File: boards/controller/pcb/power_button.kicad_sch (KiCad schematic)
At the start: 13 parts, among them Q6001 BSS138

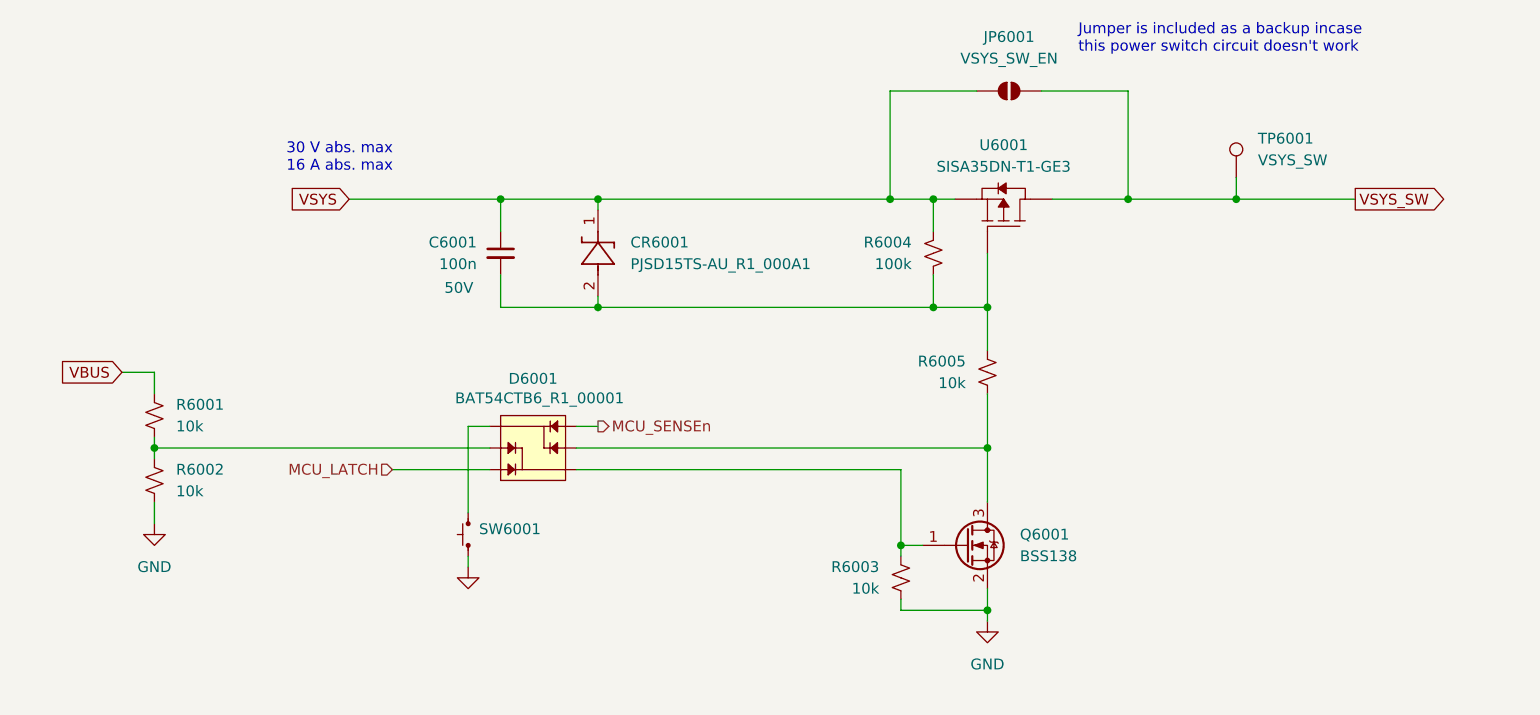
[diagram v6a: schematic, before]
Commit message: controller: Update BOM
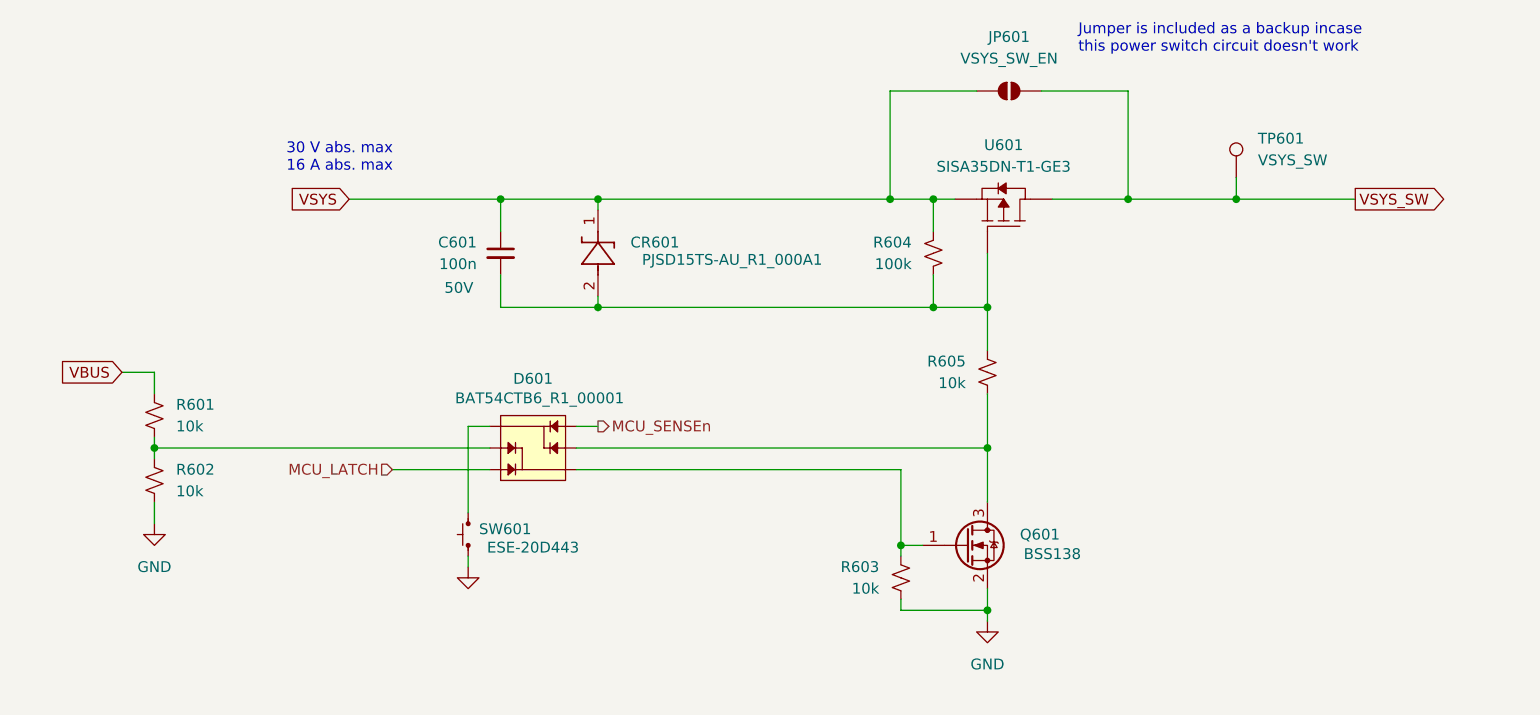
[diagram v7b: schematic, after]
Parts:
- CR601: renamed from CR6001; MPN (none) -> PJSD15TS-AU_R1_000A1
- Q601: renamed from Q6001; MPN (none) -> BSS138
- SW601: renamed from SW6001; MPN (none) -> ESE-20D443
- renumbered C6001 to C601, D6001 to D601, JP6001 to JP601, R6001 to R601, R6002 to R602, R6003 to R603, R6004 to R604, R6005 to R605, TP6001 to TP601, U6001 to U601
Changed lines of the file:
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@@
 		(on_board yes)
 		(dnp no)
-		(fields_autoplaced yes)
-		(property "Reference" "SW6001"
+		(property "Reference" "SW601"
 			(at 123.19 107.3149 90)
 			(effects
@@
 			)
 		)
+		(property "MPN" "ESE-20D443"
+			(at 129.54 109.474 90)
+			(effects
+				(font
+					(size 1.27 1.27)
+				)
+			)
+		)
+		(property "TCC" ""
+			(at 121.92 110.49 0)
+			(effects
+				(font
+					(size 1.27 1.27)
+				)
+			)
+		)
+		(property "Tolerance" ""
+			(at 121.92 110.49 0)
+			(effects
+				(font
+					(size 1.27 1.27)
+				)
+			)
+		)
+		(property "Voltage" ""
+			(at 121.92 110.49 0)
+			(effects
+				(font
+					(size 1.27 1.27)
+				)
+			)
+		)
+		(property "Package" ""
+			(at 121.92 110.49 0)
+			(effects
+				(font
+					(size 1.27 1.27)
+				)
+			)
+		)
+		(property "Power" ""
+			(at 121.92 110.49 0)
+			(effects
+				(font
+					(size 1.27 1.27)
+				)
+			)
+		)
 		(pin "2"
 		)
@@
 			(project "controller"
 				(path "/5caba13a-97ae-46d4-856f-900b12012fd8/e9c1830f-f16f-4f1e-b4e4-1e9230890439"
-					(reference "SW6001")
+					(reference "SW601")
 					(unit 1)
 				)
@@
 		(dnp no)
 		(fields_autoplaced yes)
-		(property "Reference" "JP6001"
+		(property "Reference" "JP601"
 			(at 185.42 49.53 0)
 			(effects
@@
 			(project ""
 				(path "/5caba13a-97ae-46d4-856f-900b12012fd8/e9c1830f-f16f-4f1e-b4e4-1e9230890439"
-					(reference "JP6001")
+					(reference "JP601")
 					(unit 1)
 				)
@@
 		(dnp no)
 		(fields_autoplaced yes)
-		(property "Reference" "#PWR06001"
+		(property "Reference" "#PWR0601"
 			(at 85.09 113.03 0)
 			(effects
@@
 			(project "controller"
 				(path "/5caba13a-97ae-46d4-856f-900b12012fd8/e9c1830f-f16f-4f1e-b4e4-1e9230890439"
-					(reference "#PWR06001")
+					(reference "#PWR0601")
 					(unit 1)
 				)
@@
 		(on_board yes)
 		(dnp no)
-		(property "Reference" "R6004"
+		(property "Reference" "R604"
 			(at 173.99 73.6599 0)
 			(effects
@@
 			(project "controller"
 				(path "/5caba13a-97ae-46d4-856f-900b12012fd8/e9c1830f-f16f-4f1e-b4e4-1e9230890439"
-					(reference "R6004")
+					(reference "R604")
 					(unit 1)
 				)
@@
 		(dnp no)
 		(fields_autoplaced yes)
-		(property "Reference" "TP6001"
+		(property "Reference" "TP601"
 			(at 214.63 61.4679 0)
 			(effects
@@
 			(project "controller"
 				(path "/5caba13a-97ae-46d4-856f-900b12012fd8/e9c1830f-f16f-4f1e-b4e4-1e9230890439"
-					(reference "TP6001")
+					(reference "TP601")
 					(unit 1)
 				)
@@
 		(dnp no)
 		(fields_autoplaced yes)
-		(property "Reference" "U6001"
+		(property "Reference" "U601"
 			(at 184.785 62.23 90)
 			(effects
@@
 			(project ""
 				(path "/5caba13a-97ae-46d4-856f-900b12012fd8/e9c1830f-f16f-4f1e-b4e4-1e9230890439"
-					(reference "U6001")
+					(reference "U601")
 					(unit 1)
 				)
@@
 		(on_board yes)
 		(dnp no)
-		(property "Reference" "Q6001"
+		(property "Reference" "Q601"
 			(at 186.69 107.9499 0)
 			(effects
@@
 				)
 				(justify left)
+				(hide yes)
 			)
 		)
@@
 			)
 		)
+		(property "MPN" "BSS138"
+			(at 190.5 110.236 0)
+			(effects
+				(font
+					(size 1.27 1.27)
+				)
+			)
+		)
+		(property "TCC" ""
+			(at 180.34 109.22 0)
+			(effects
+				(font
+					(size 1.27 1.27)
+				)
+			)
+		)
+		(property "Tolerance" ""
+			(at 180.34 109.22 0)
+			(effects
+				(font
+					(size 1.27 1.27)
+				)
+			)
+		)
+		(property "Voltage" ""
+			(at 180.34 109.22 0)
+			(effects
+				(font
+					(size 1.27 1.27)
+				)
+			)
+		)
+		(property "Package" ""
+			(at 180.34 109.22 0)
+			(effects
+				(font
+					(size 1.27 1.27)
+				)
+			)
+		)
+		(property "Power" ""
+			(at 180.34 109.22 0)
+			(effects
+				(font
+					(size 1.27 1.27)
+				)
+			)
+		)
 		(pin "2"
 		)
@@
 			(project "controller"
 				(path "/5caba13a-97ae-46d4-856f-900b12012fd8/e9c1830f-f16f-4f1e-b4e4-1e9230890439"
-					(reference "Q6001")
+					(reference "Q601")
 					(unit 1)
 				)
@@
 		(dnp no)
 		(fields_autoplaced yes)
-		(property "Reference" "R6002"
+		(property "Reference" "R602"
 			(at 87.63 100.3299 0)
 			(effects
@@
 			(project "controller"
 				(path "/5caba13a-97ae-46d4-856f-900b12012fd8/e9c1830f-f16f-4f1e-b4e4-1e9230890439"
-					(reference "R6002")
+					(reference "R602")
 					(unit 1)
 				)
@@
 		(dnp no)
 		(fields_autoplaced yes)
-		(property "Reference" "#PWR06003"
+		(property "Reference" "#PWR0603"
 			(at 182.88 124.46 0)
 			(effects
@@
 			(project "controller"
 				(path "/5caba13a-97ae-46d4-856f-900b12012fd8/e9c1830f-f16f-4f1e-b4e4-1e9230890439"
-					(reference "#PWR06003")
+					(reference "#PWR0603")
 					(unit 1)
 				)
@@
 		(on_board yes)
 		(dnp no)
-		(property "Reference" "R6003"
+		(property "Reference" "R603"
 			(at 170.18 111.7599 0)
 			(effects
@@
 			(project "controller"
 				(path "/5caba13a-97ae-46d4-856f-900b12012fd8/e9c1830f-f16f-4f1e-b4e4-1e9230890439"
-					(reference "R6003")
+					(reference "R603")
 					(unit 1)
 				)
@@
 		(dnp no)
 		(fields_autoplaced yes)
-		(property "Reference" "#PWR06002"
+		(property "Reference" "#PWR0602"
 			(at 121.92 118.11 0)
 			(effects
@@
 			(project "controller"
 				(path "/5caba13a-97ae-46d4-856f-900b12012fd8/e9c1830f-f16f-4f1e-b4e4-1e9230890439"
-					(reference "#PWR06002")
+					(reference "#PWR0602")
 					(unit 1)
 				)
@@
 		(dnp no)
 		(fields_autoplaced yes)
-		(property "Reference" "R6001"
+		(property "Reference" "R601"
 			(at 87.63 92.7099 0)
 			(effects
@@
 			(project "controller"
 				(path "/5caba13a-97ae-46d4-856f-900b12012fd8/e9c1830f-f16f-4f1e-b4e4-1e9230890439"
-					(reference "R6001")
+					(reference "R601")
 					(unit 1)
 				)
@@
 		(on_board yes)
 		(dnp no)
-		(property "Reference" "D6001"
+		(property "Reference" "D601"
 			(at 129.54 89.662 0)
 			(effects
@@
 			(project "controller"
 				(path "/5caba13a-97ae-46d4-856f-900b12012fd8/e9c1830f-f16f-4f1e-b4e4-1e9230890439"
-					(reference "D6001")
+					(reference "D601")
 					(unit 1)
 				)
@@
 		(on_board yes)
 		(dnp no)
-		(property "Reference" "C6001"
+		(property "Reference" "C601"
 			(at 122.936 73.66 0)
 			(effects
@@
 			(project "controller"
 				(path "/5caba13a-97ae-46d4-856f-900b12012fd8/e9c1830f-f16f-4f1e-b4e4-1e9230890439"
-					(reference "C6001")
+					(reference "C601")
 					(unit 1)
 				)
@@
 		(on_board yes)
 		(dnp no)
-		(fields_autoplaced yes)
-		(property "Reference" "CR6001"
+		(property "Reference" "CR601"
 			(at 140.97 73.6599 90)
 			(effects
@@
 				)
 				(justify right)
+				(hide yes)
 			)
 		)
@@
 			)
 		)
-		(property "MPN" ""
-			(at 137.16 80.01 0)
+		(property "MPN" "PJSD15TS-AU_R1_000A1"
+			(at 152.908 75.692 90)
 			(effects
 				(font
@@
 			(project ""
 				(path "/5caba13a-97ae-46d4-856f-900b12012fd8/e9c1830f-f16f-4f1e-b4e4-1e9230890439"
-					(reference "CR6001")
+					(reference "CR601")
 					(unit 1)
 				)
@@
 		(on_board yes)
 		(dnp no)
-		(property "Reference" "R6005"
+		(property "Reference" "R605"
 			(at 180.34 87.6299 0)
 			(effects
@@
 			(project "controller"
 				(path "/5caba13a-97ae-46d4-856f-900b12012fd8/e9c1830f-f16f-4f1e-b4e4-1e9230890439"
-					(reference "R6005")
-					(unit 1)
-				)
+					(reference "R605")
+					(unit 1)
+				)
